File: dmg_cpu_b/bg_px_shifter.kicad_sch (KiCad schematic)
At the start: 97 parts

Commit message: All sheets captured. Serious tidying is required in PPU section.
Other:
- company: (none) -> CC-BY-SA-4.0 Régis Galland & Michael Singer -- Derived work from Furrtek
- title: (none) -> DMG CPU B

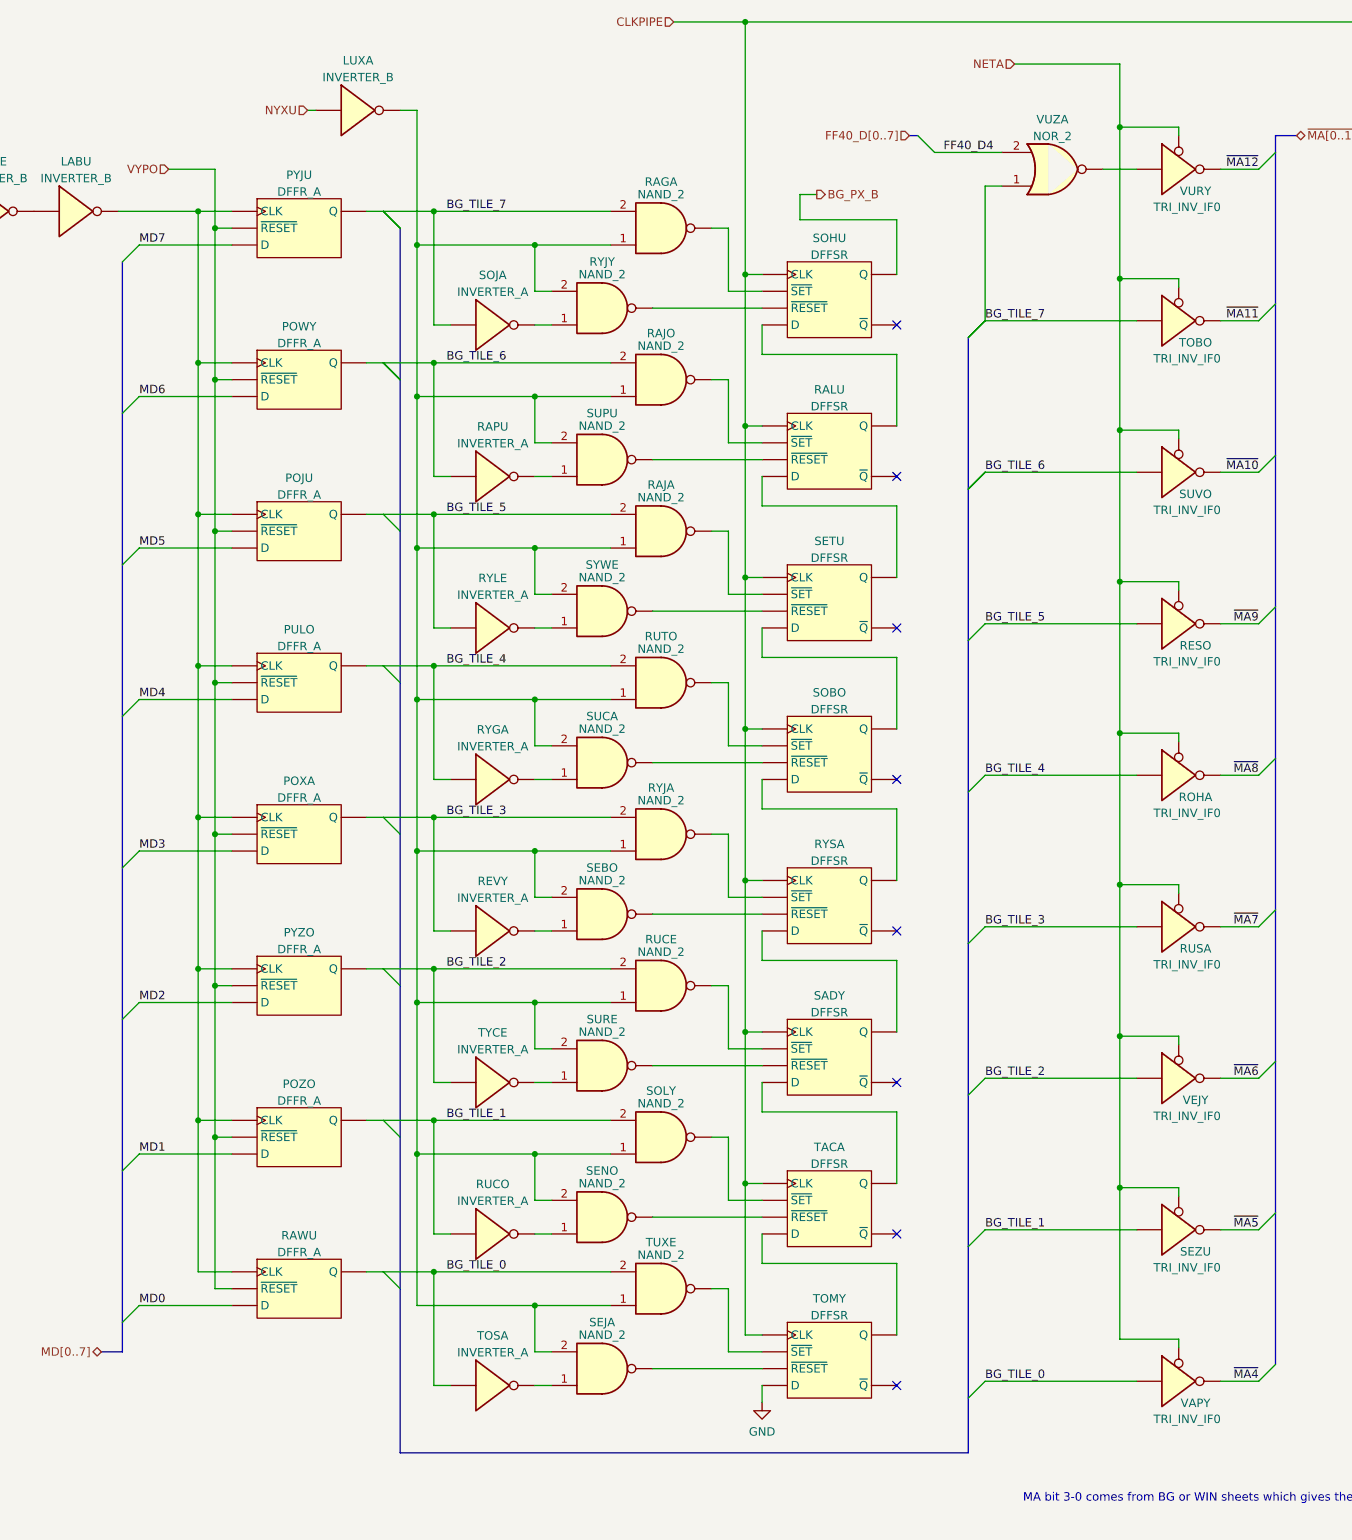
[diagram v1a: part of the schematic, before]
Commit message: New sheet created to free up space on LCD and SCX/SCY sheets and joined common signals.
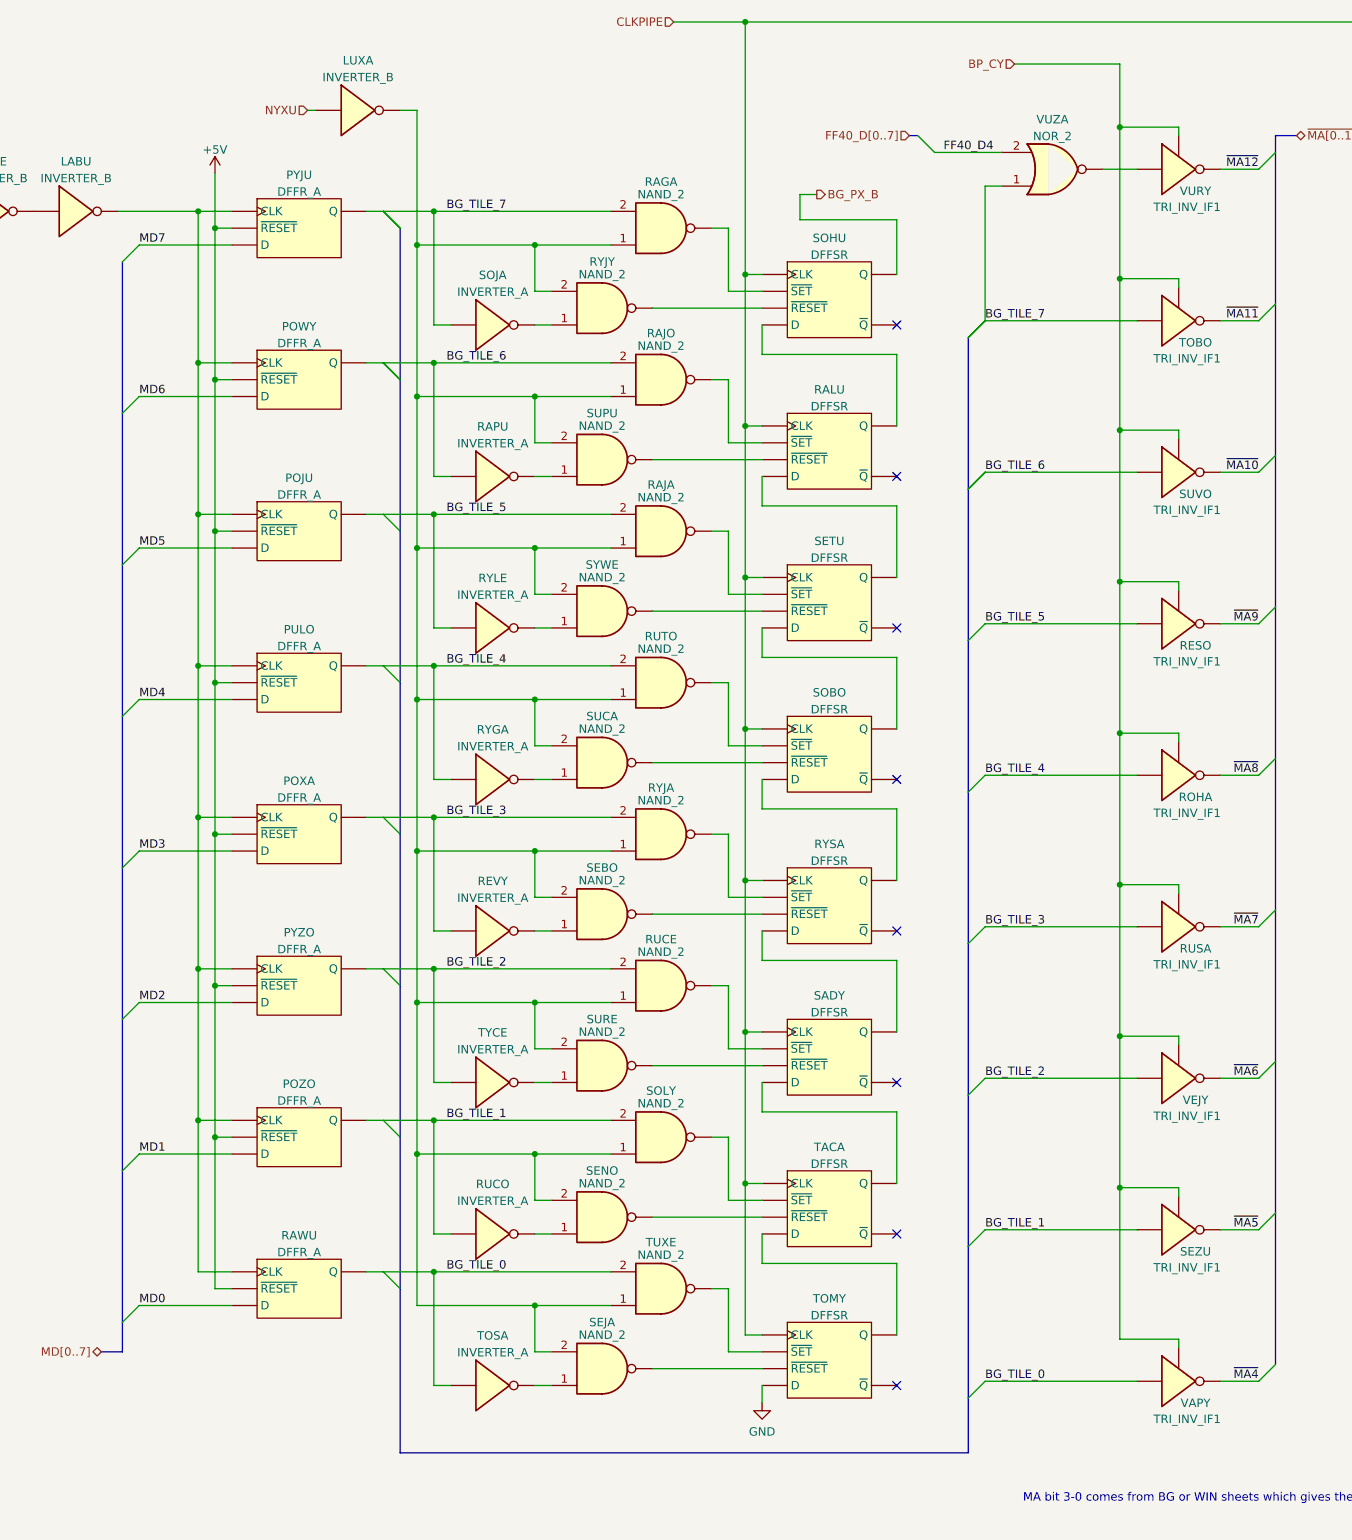
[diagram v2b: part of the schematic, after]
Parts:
- RESO, ROHA, RUSA, SEZU, SUVO, TOBO, VAPY, VEJY, VURY: value TRI_INV_IF0 -> TRI_INV_IF1; symbol DMG_CPU_Cells:TRI_INV_IF0 -> DMG_CPU_Cells:TRI_INV_IF1
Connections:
- net NETA renamed BP_CY
- net VYPO renamed +5V
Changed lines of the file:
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@@
-    (stroke (width 0) (type default) (color 0 0 0 0))
-  )
-  (wire (pts (xy 67.945 47.625) (xy 74.93 47.625))
     (stroke (width 0) (type default) (color 0 0 0 0))
   )
@@
     (stroke (width 0) (type default) (color 0 0 0 0))
   )
-  (wire (pts (xy 74.93 56.515) (xy 74.93 47.625))
+  (wire (pts (xy 74.93 56.515) (xy 74.93 48.26))
     (stroke (width 0) (type default) (color 0 0 0 0))
   )
@@
     (effects (font (size 1.27 1.27)) (justify right))
   )
-  (hierarchical_label "NETA" (shape input) (at 195.58 31.75 180)
+  (hierarchical_label "BP_CY" (shape input) (at 195.58 31.75 180)
     (effects (font (size 1.27 1.27)) (justify right))
   )
@@
   )
   (hierarchical_label "NYDY" (shape input) (at 263.525 53.975 180)
-    (effects (font (size 1.27 1.27)) (justify right))
-  )
-  (hierarchical_label "VYPO" (shape input) (at 67.945 47.625 180)
     (effects (font (size 1.27 1.27)) (justify right))
   )
@@
     (pin "2")
   )
-  (symbol (lib_id "DMG_CPU_Cells:TRI_INV_IF0") (at 220.345 139.065 0) (unit 1)
+  (symbol (lib_id "DMG_CPU_Cells:TRI_INV_IF1") (at 220.345 139.065 0) (unit 1)
     (in_bom yes) (on_board yes)
     (property "Reference" "ROHA" (id 0) (at 222.885 142.367 0))
-    (property "Value" "TRI_INV_IF0" (id 1) (at 221.615 144.78 0))
+    (property "Value" "TRI_INV_IF1" (id 1) (at 221.615 144.78 0))
     (property "Footprint" "" (id 2) (at 217.805 139.065 0)
       (effects (font (size 1.27 1.27)) hide)
     )
-    (property "Datasheet" "http://iceboy.a-singer.de/doc/dmg_cells.html#tri_inv_if0" (id 3) (at 221.615 149.225 0)
-      (effects (font (size 1.27 1.27)) hide)
-    )
-    (pin "2")
-    (pin "3")
-    (pin "1")
-  )
-  (symbol (lib_id "DMG_CPU_Cells:TRI_INV_IF0") (at 220.345 230.505 0) (unit 1)
+    (property "Datasheet" "http://iceboy.a-singer.de/doc/dmg_cells.html#tri_inv_if1" (id 3) (at 221.615 149.225 0)
+      (effects (font (size 1.27 1.27)) hide)
+    )
+    (pin "2")
+    (pin "3")
+    (pin "1")
+  )
+  (symbol (lib_id "DMG_CPU_Cells:TRI_INV_IF1") (at 220.345 230.505 0) (unit 1)
     (in_bom yes) (on_board yes)
     (property "Reference" "VAPY" (id 0) (at 222.885 233.807 0))
-    (property "Value" "TRI_INV_IF0" (id 1) (at 221.615 236.22 0))
+    (property "Value" "TRI_INV_IF1" (id 1) (at 221.615 236.22 0))
     (property "Footprint" "" (id 2) (at 217.805 230.505 0)
       (effects (font (size 1.27 1.27)) hide)
     )
-    (property "Datasheet" "http://iceboy.a-singer.de/doc/dmg_cells.html#tri_inv_if0" (id 3) (at 221.615 240.665 0)
+    (property "Datasheet" "http://iceboy.a-singer.de/doc/dmg_cells.html#tri_inv_if1" (id 3) (at 221.615 240.665 0)
       (effects (font (size 1.27 1.27)) hide)
     )
@@
     (pin "7")
   )
-  (symbol (lib_id "DMG_CPU_Cells:TRI_INV_IF0") (at 220.345 70.485 0) (unit 1)
+  (symbol (lib_id "DMG_CPU_Cells:TRI_INV_IF1") (at 220.345 70.485 0) (unit 1)
     (in_bom yes) (on_board yes)
     (property "Reference" "TOBO" (id 0) (at 222.885 73.787 0))
-    (property "Value" "TRI_INV_IF0" (id 1) (at 221.615 76.2 0))
+    (property "Value" "TRI_INV_IF1" (id 1) (at 221.615 76.2 0))
     (property "Footprint" "" (id 2) (at 217.805 70.485 0)
       (effects (font (size 1.27 1.27)) hide)
     )
-    (property "Datasheet" "http://iceboy.a-singer.de/doc/dmg_cells.html#tri_inv_if0" (id 3) (at 221.615 80.645 0)
+    (property "Datasheet" "http://iceboy.a-singer.de/doc/dmg_cells.html#tri_inv_if1" (id 3) (at 221.615 80.645 0)
       (effects (font (size 1.27 1.27)) hide)
     )
@@
     (pin "6")
   )
-  (symbol (lib_id "DMG_CPU_Cells:TRI_INV_IF0") (at 220.345 207.645 0) (unit 1)
+  (symbol (lib_id "DMG_CPU_Cells:TRI_INV_IF1") (at 220.345 207.645 0) (unit 1)
     (in_bom yes) (on_board yes)
     (property "Reference" "SEZU" (id 0) (at 222.885 210.947 0))
-    (property "Value" "TRI_INV_IF0" (id 1) (at 221.615 213.36 0))
+    (property "Value" "TRI_INV_IF1" (id 1) (at 221.615 213.36 0))
     (property "Footprint" "" (id 2) (at 217.805 207.645 0)
       (effects (font (size 1.27 1.27)) hide)
     )
-    (property "Datasheet" "http://iceboy.a-singer.de/doc/dmg_cells.html#tri_inv_if0" (id 3) (at 221.615 217.805 0)
+    (property "Datasheet" "http://iceboy.a-singer.de/doc/dmg_cells.html#tri_inv_if1" (id 3) (at 221.615 217.805 0)
       (effects (font (size 1.27 1.27)) hide)
     )
@@
     (pin "3")
   )
-  (symbol (lib_id "DMG_CPU_Cells:TRI_INV_IF0") (at 220.345 93.345 0) (unit 1)
+  (symbol (lib_id "DMG_CPU_Cells:TRI_INV_IF1") (at 220.345 93.345 0) (unit 1)
     (in_bom yes) (on_board yes)
     (property "Reference" "SUVO" (id 0) (at 222.885 96.647 0))
-    (property "Value" "TRI_INV_IF0" (id 1) (at 221.615 99.06 0))
+    (property "Value" "TRI_INV_IF1" (id 1) (at 221.615 99.06 0))
     (property "Footprint" "" (id 2) (at 217.805 93.345 0)
       (effects (font (size 1.27 1.27)) hide)
     )
-    (property "Datasheet" "http://iceboy.a-singer.de/doc/dmg_cells.html#tri_inv_if0" (id 3) (at 221.615 103.505 0)
+    (property "Datasheet" "http://iceboy.a-singer.de/doc/dmg_cells.html#tri_inv_if1" (id 3) (at 221.615 103.505 0)
       (effects (font (size 1.27 1.27)) hide)
     )
@@
     (pin "2")
   )
-  (symbol (lib_id "DMG_CPU_Cells:TRI_INV_IF0") (at 220.345 184.785 0) (unit 1)
+  (symbol (lib_id "DMG_CPU_Cells:TRI_INV_IF1") (at 220.345 184.785 0) (unit 1)
     (in_bom yes) (on_board yes)
     (property "Reference" "VEJY" (id 0) (at 222.885 188.087 0))
-    (property "Value" "TRI_INV_IF0" (id 1) (at 221.615 190.5 0))
+    (property "Value" "TRI_INV_IF1" (id 1) (at 221.615 190.5 0))
     (property "Footprint" "" (id 2) (at 217.805 184.785 0)
       (effects (font (size 1.27 1.27)) hide)
     )
-    (property "Datasheet" "http://iceboy.a-singer.de/doc/dmg_cells.html#tri_inv_if0" (id 3) (at 221.615 194.945 0)
+    (property "Datasheet" "http://iceboy.a-singer.de/doc/dmg_cells.html#tri_inv_if1" (id 3) (at 221.615 194.945 0)
       (effects (font (size 1.27 1.27)) hide)
     )
@@
     (pin "7")
   )
-  (symbol (lib_id "DMG_CPU_Cells:TRI_INV_IF0") (at 220.345 161.925 0) (unit 1)
+  (symbol (lib_id "DMG_CPU_Cells:TRI_INV_IF1") (at 220.345 161.925 0) (unit 1)
     (in_bom yes) (on_board yes)
     (property "Reference" "RUSA" (id 0) (at 222.885 165.227 0))
-    (property "Value" "TRI_INV_IF0" (id 1) (at 221.615 167.64 0))
+    (property "Value" "TRI_INV_IF1" (id 1) (at 221.615 167.64 0))
     (property "Footprint" "" (id 2) (at 217.805 161.925 0)
       (effects (font (size 1.27 1.27)) hide)
     )
-    (property "Datasheet" "http://iceboy.a-singer.de/doc/dmg_cells.html#tri_inv_if0" (id 3) (at 221.615 172.085 0)
+    (property "Datasheet" "http://iceboy.a-singer.de/doc/dmg_cells.html#tri_inv_if1" (id 3) (at 221.615 172.085 0)
       (effects (font (size 1.27 1.27)) hide)
     )
@@
     (pin "4")
   )
-  (symbol (lib_id "DMG_CPU_Cells:TRI_INV_IF0") (at 220.345 47.625 0) (unit 1)
+  (symbol (lib_id "DMG_CPU_Cells:TRI_INV_IF1") (at 220.345 47.625 0) (unit 1)
     (in_bom yes) (on_board yes)
     (property "Reference" "VURY" (id 0) (at 222.885 50.927 0))
-    (property "Value" "TRI_INV_IF0" (id 1) (at 221.615 53.34 0))
+    (property "Value" "TRI_INV_IF1" (id 1) (at 221.615 53.34 0))
     (property "Footprint" "" (id 2) (at 217.805 47.625 0)
       (effects (font (size 1.27 1.27)) hide)
     )
-    (property "Datasheet" "http://iceboy.a-singer.de/doc/dmg_cells.html#tri_inv_if0" (id 3) (at 221.615 57.785 0)
+    (property "Datasheet" "http://iceboy.a-singer.de/doc/dmg_cells.html#tri_inv_if1" (id 3) (at 221.615 57.785 0)
       (effects (font (size 1.27 1.27)) hide)
     )
@@
     (pin "3")
   )
-  (symbol (lib_id "DMG_CPU_Cells:TRI_INV_IF0") (at 220.345 116.205 0) (unit 1)
+  (symbol (lib_id "DMG_CPU_Cells:TRI_INV_IF1") (at 220.345 116.205 0) (unit 1)
     (in_bom yes) (on_board yes)
     (property "Reference" "RESO" (id 0) (at 222.885 119.507 0))
-    (property "Value" "TRI_INV_IF0" (id 1) (at 221.615 121.92 0))
+    (property "Value" "TRI_INV_IF1" (id 1) (at 221.615 121.92 0))
     (property "Footprint" "" (id 2) (at 217.805 116.205 0)
       (effects (font (size 1.27 1.27)) hide)
     )
-    (property "Datasheet" "http://iceboy.a-singer.de/doc/dmg_cells.html#tri_inv_if0" (id 3) (at 221.615 126.365 0)
+    (property "Datasheet" "http://iceboy.a-singer.de/doc/dmg_cells.html#tri_inv_if1" (id 3) (at 221.615 126.365 0)
       (effects (font (size 1.27 1.27)) hide)
     )
@@
     (pin "3")
   )
+  (symbol (lib_id "power:+5V") (at 74.93 48.26 0) (unit 1)
+    (in_bom yes) (on_board yes) (fields_autoplaced)
+    (property "Reference" "#PWR?" (id 0) (at 74.93 52.07 0)
+      (effects (font (size 1.27 1.27)) hide)
+    )
+    (property "Value" "+5V" (id 1) (at 74.93 44.6842 0))
+    (property "Footprint" "" (id 2) (at 74.93 48.26 0)
+      (effects (font (size 1.27 1.27)) hide)
+    )
+    (property "Datasheet" "" (id 3) (at 74.93 48.26 0)
+      (effects (font (size 1.27 1.27)) hide)
+    )
+    (pin "1")
+  )
   (symbol (lib_id "DMG_CPU_Cells:INVERTER_A") (at 116.84 231.14 0) (unit 1)

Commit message: Fixes based on review. + various other edits.
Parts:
- added LOMA_INV: INVERTER_A, symbol DMG_CPU_Cells:INVERTER_A
- renumbered MOSY to MYVY
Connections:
- net at LEGU.1 (~{ENA}), LEGU.3 (ENA), LUZO.1 (~{ENA})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: now also LOMA_INV.2; no longer LOMA.2
- new net: LOMA.2, LOMA_INV.1
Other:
- moved on the sheet: LOMA, METE
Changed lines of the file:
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@@
+    (stroke (width 0) (type default) (color 0 0 0 0))
+  )
+  (wire (pts (xy 290.195 53.975) (xy 296.545 53.975))
     (stroke (width 0) (type default) (color 0 0 0 0))
   )
@@
     (stroke (width 0) (type default) (color 0 0 0 0))
   )
-  (wire (pts (xy 290.195 53.975) (xy 296.545 53.975))
-    (stroke (width 0) (type default) (color 0 0 0 0))
-  )
   (wire (pts (xy 324.485 59.055) (xy 342.265 59.055))
     (stroke (width 0) (type default) (color 0 0 0 0))
@@
     (stroke (width 0) (type default) (color 0 0 0 0))
   )
-  (wire (pts (xy 263.525 53.975) (xy 264.795 53.975))
+  (wire (pts (xy 250.825 53.975) (xy 252.095 53.975))
     (stroke (width 0) (type default) (color 0 0 0 0))
   )
@@
     (effects (font (size 1.27 1.27)) (justify right))
   )
-  (hierarchical_label "NYDY" (shape input) (at 263.525 53.975 180)
+  (hierarchical_label "NYDY" (shape input) (at 250.825 53.975 180)
     (effects (font (size 1.27 1.27)) (justify right))
   )
@@
   (symbol (lib_id "DMG_CPU_Cells:NAND_2") (at 361.315 125.095 0) (mirror x) (unit 1)
     (in_bom yes) (on_board yes)
-    (property "Reference" "MOSY" (id 0) (at 361.315 118.11 0))
+    (property "Reference" "MYVY" (id 0) (at 361.315 118.11 0))
     (property "Value" "NAND_2" (id 1) (at 361.315 120.015 0))
     (property "Footprint" "" (id 2) (at 361.315 125.095 0)
@@
     (pin "1")
   )
-  (symbol (lib_id "DMG_CPU_Cells:INVERTER_A") (at 271.145 53.975 0) (unit 1)
-    (in_bom yes) (on_board yes) (fields_autoplaced)
-    (property "Reference" "METE" (id 0) (at 271.145 46.4652 0))
-    (property "Value" "INVERTER_A" (id 1) (at 271.145 49.0021 0))
-    (property "Footprint" "" (id 2) (at 268.605 53.975 0)
-      (effects (font (size 1.27 1.27)) hide)
-    )
-    (property "Datasheet" "http://iceboy.a-singer.de/doc/dmg_cells.html#inv_a" (id 3) (at 272.415 61.595 0)
+  (symbol (lib_id "DMG_CPU_Cells:INVERTER_A") (at 258.445 53.975 0) (unit 1)
+    (in_bom yes) (on_board yes) (fields_autoplaced)
+    (property "Reference" "METE" (id 0) (at 258.445 46.4652 0))
+    (property "Value" "INVERTER_A" (id 1) (at 258.445 49.0021 0))
+    (property "Footprint" "" (id 2) (at 255.905 53.975 0)
+      (effects (font (size 1.27 1.27)) hide)
+    )
+    (property "Datasheet" "http://iceboy.a-singer.de/doc/dmg_cells.html#inv_a" (id 3) (at 259.715 61.595 0)
       (effects (font (size 1.27 1.27)) hide)
     )
@@
     (pin "1")
   )
-  (symbol (lib_id "DMG_CPU_Cells:INVERTER_A") (at 283.845 53.975 0) (unit 1)
-    (in_bom yes) (on_board yes) (fields_autoplaced)
-    (property "Reference" "LOMA" (id 0) (at 283.845 46.4652 0))
-    (property "Value" "INVERTER_A" (id 1) (at 283.845 49.0021 0))
-    (property "Footprint" "" (id 2) (at 281.305 53.975 0)
-      (effects (font (size 1.27 1.27)) hide)
-    )
-    (property "Datasheet" "http://iceboy.a-singer.de/doc/dmg_cells.html#inv_a" (id 3) (at 285.115 61.595 0)
+  (symbol (lib_id "DMG_CPU_Cells:INVERTER_A") (at 271.145 53.975 0) (unit 1)
+    (in_bom yes) (on_board yes) (fields_autoplaced)
+    (property "Reference" "LOMA" (id 0) (at 271.145 46.4652 0))
+    (property "Value" "INVERTER_A" (id 1) (at 271.145 49.0021 0))
+    (property "Footprint" "" (id 2) (at 268.605 53.975 0)
+      (effects (font (size 1.27 1.27)) hide)
+    )
+    (property "Datasheet" "http://iceboy.a-singer.de/doc/dmg_cells.html#inv_a" (id 3) (at 272.415 61.595 0)
       (effects (font (size 1.27 1.27)) hide)
     )
@@
     (pin "4")
   )
+  (symbol (lib_id "DMG_CPU_Cells:INVERTER_A") (at 283.845 53.975 0) (unit 1)
+    (in_bom yes) (on_board yes) (fields_autoplaced)
+    (property "Reference" "LOMA_INV" (id 0) (at 283.845 46.4652 0))
+    (property "Value" "INVERTER_A" (id 1) (at 283.845 49.0021 0))
+    (property "Footprint" "" (id 2) (at 281.305 53.975 0)
+      (effects (font (size 1.27 1.27)) hide)
+    )
+    (property "Datasheet" "http://iceboy.a-singer.de/doc/dmg_cells.html#inv_a" (id 3) (at 285.115 61.595 0)
+      (effects (font (size 1.27 1.27)) hide)
+    )
+    (pin "1")
+    (pin "2")
+  )
   (symbol (lib_id "DMG_CPU_Cells:NAND_2") (at 361.315 216.535 0) (mirror x) (unit 1)
